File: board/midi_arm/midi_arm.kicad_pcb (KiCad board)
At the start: 2 copper layers, 100 x 100 mm, 24 parts, among them J2 Conn_01x03_Pin, J3 Conn_01x04_Pin, J4 Conn_01x05_Pin, SW1 SW_MEC_5E, SW2 SW_DIP_x01

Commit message: rev 4 board
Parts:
- removed J2: Conn_01x03_Pin, midi_arm:LED_conn
- removed J3: Conn_01x04_Pin, Connector_PinHeader_2.54mm:PinHeader_1x04_P2.54mm_Vertical
- removed R15: 0k, Resistor_SMD:R_0805_2012Metric_Pad1.20x1.40mm_HandSolder
- removed R16: 24K, Resistor_SMD:R_0805_2012Metric_Pad1.20x1.40mm_HandSolder
- added J1: Conn_01x06_Socket, Connector_PinHeader_2.54mm:PinHeader_1x06_P2.54mm_Vertical, F.Cu at (173.5, 97.0)
- R1, R13, R14, R2, R3, R4, R5, R7, R8, R9, U1, U2, U4: moved to B.Cu
- U3: moved to F.Cu
- moved R4 38.9 mm to (154.0, 118.5)
- moved R9 34.9 mm to (151.3, 108.2)
- moved R3 34.1 mm to (151.2, 117.7), turned to 90 degrees
- moved R8 33.3 mm to (158.0, 117.5), turned to 180 degrees
- moved R14 31.8 mm to (151.2, 112.7), turned to -90 degrees
- moved R2 30.9 mm to (158.0, 120.5)
- moved U1 26.9 mm to (156.5, 113.1), turned to 0 degrees
- moved R1 26.1 mm to (161.5, 116.8), turned to -90 degrees
- moved R13 25.6 mm to (162.4, 109.6), turned to 90 degrees
- moved H1 22.5 mm to (169.0, 96.9)
- moved U4 20.8 mm to (160.1, 101.1)
- moved R7 19.7 mm to (152.0, 101.5), turned to -90 degrees
- moved J4 19.6 mm to (151.8, 97.0)
- moved R5 14.6 mm to (161.5, 101.5), turned to -90 degrees
- moved SW2 8.72 mm to (156.8, 100.7), turned to 0 degrees
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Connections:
- U2 pad 8: Net-(U2-INT) -> unconnected-(U2-INT-Pad8)
- U3 pad 14: Net-(U3-GPIO10) -> Net-(D1-DIN)
- U4 pad 7: Net-(U2-INT) -> unconnected-(U4-A_INT1-Pad7)
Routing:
- net Net-(D1-DIN): track 10.4 -> 59.7 mm, vias 0 -> 1
- net Net-(U2-INT): track 35.8 -> 0.00 mm, vias 1 -> 0
- net Net-(J1-Pin_4): track 36.3 -> 12.1 mm, vias 1 -> 0
- net Net-(U3-GPIO10): track 22.9 -> 0.00 mm, vias 2 -> 0
- net /BUTTON1: track 43.4 -> 21.6 mm, vias 1 -> 0
- net Net-(U1-VinB-): track 30.6 -> 12.2 mm
- net Net-(U1-VinA+): track 37.2 -> 20.3 mm, vias 2 -> 0
- net GND1: track 130.1 -> 113.9 mm, vias 5 -> 2
- net /VCC_3V3: track 105.5 -> 89.5 mm, vias 2 -> 0
- net /BUTTON2: track 35.8 -> 22.8 mm, vias 0 -> 1
- net Net-(J1-Pin_5): track 23.2 -> 10.7 mm
- net /ADC1_1: track 24.3 -> 11.8 mm, vias 1 -> 0
- net Net-(D2-DOUT): track 8.93 -> 18.8 mm
- net /SCL: track 51.3 -> 41.8 mm, vias 2 -> 0
- net /SDA: track 30.0 -> 39.3 mm, vias 1 -> 2
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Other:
- board text added: "3V3"
- board text added: "5V"
- board text added: "BABOI V4"
- board text added: "C1"
- board text added: "C2"
- board text added: "D"
- board text added: "G"
- board text added: "LINK"
- board text added: "R1"
- board text added: "R2"
- board text added: "S1"
- board text added: "S2"
- board text added: "STATUS"
- board text removed: "+"
- board text removed: "-"
- board text removed: "BABOI"
- board text removed: "GLOVE"
- board text removed: "LED"
- board text removed: "V 3.5"

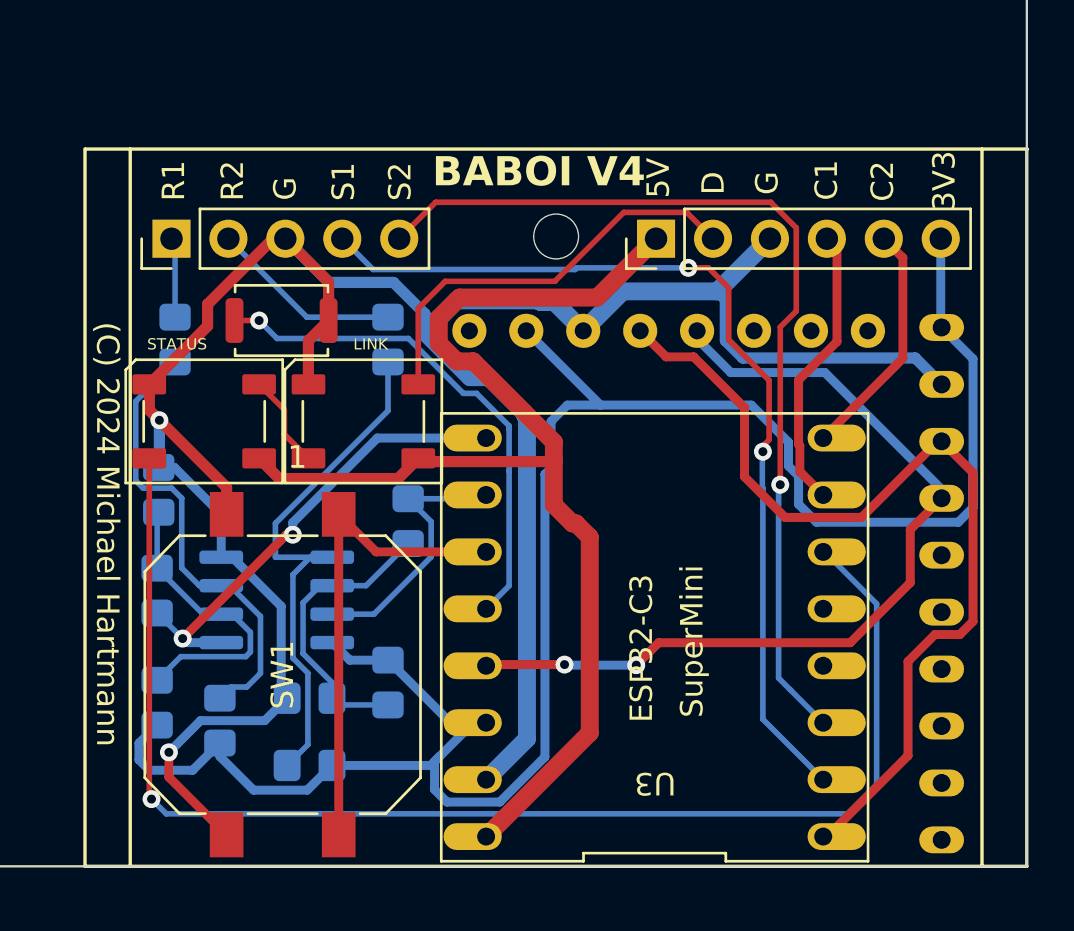
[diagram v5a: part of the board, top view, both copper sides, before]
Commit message: Adding latest PCB, adding new settings to override midi bus/uart
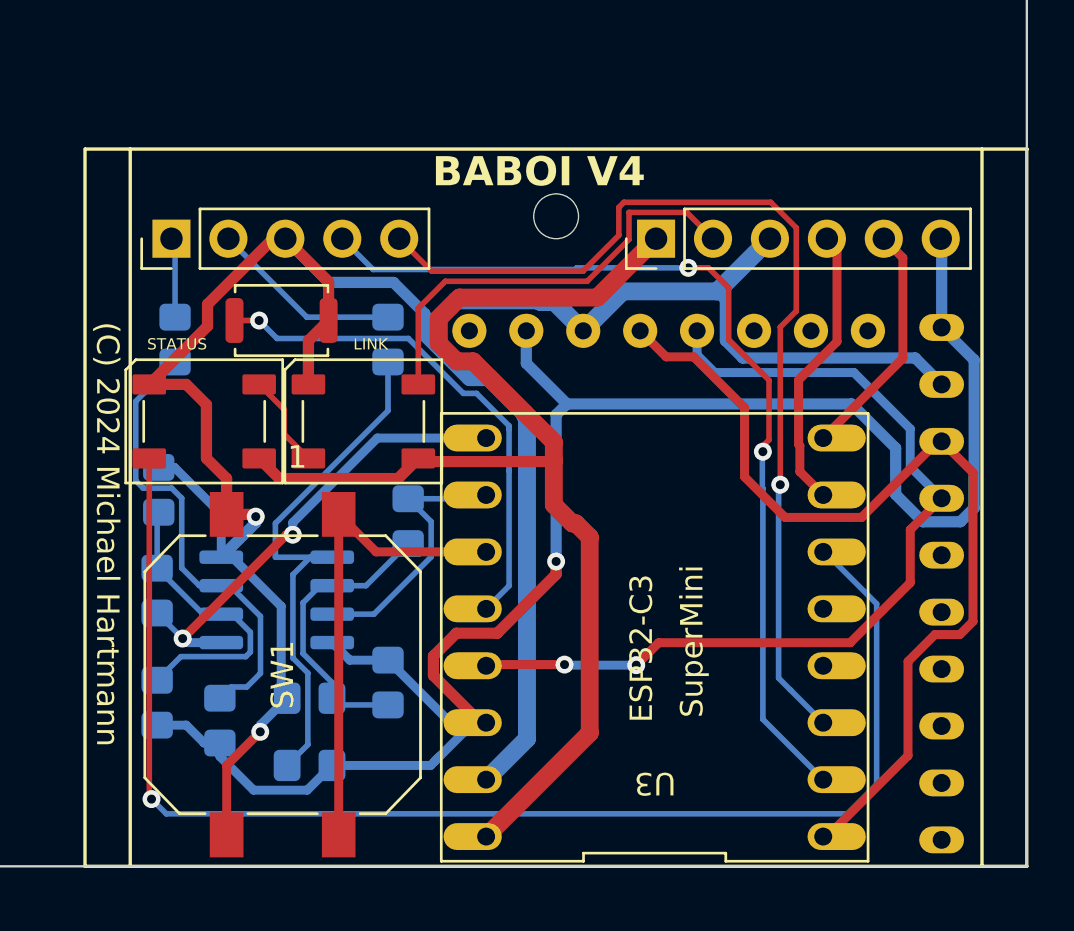
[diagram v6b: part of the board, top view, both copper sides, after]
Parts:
- moved H1 0.90 mm to (169.0, 96.0)
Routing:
- net /VCC_3V3: track 89.5 -> 81.3 mm, vias 0 -> 1
- net /SPARE2: track 42.1 -> 44.0 mm
- net GND1: track 113.9 -> 112.4 mm
- net /SDA: track 39.3 -> 40.5 mm
- net Net-(D2-DOUT): track 18.8 -> 19.5 mm
